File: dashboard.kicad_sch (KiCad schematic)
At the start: 38 parts, among them J2 Conn_01x02, J3 RJ45, J4 Conn_01x10, J5 776267-1, Q1 2N7002, SW1 SW_Push, SW2 SW_SPST, SW4 SW_SPST, U1 TPS542025DDC, U2 R-78C5.0-1.0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

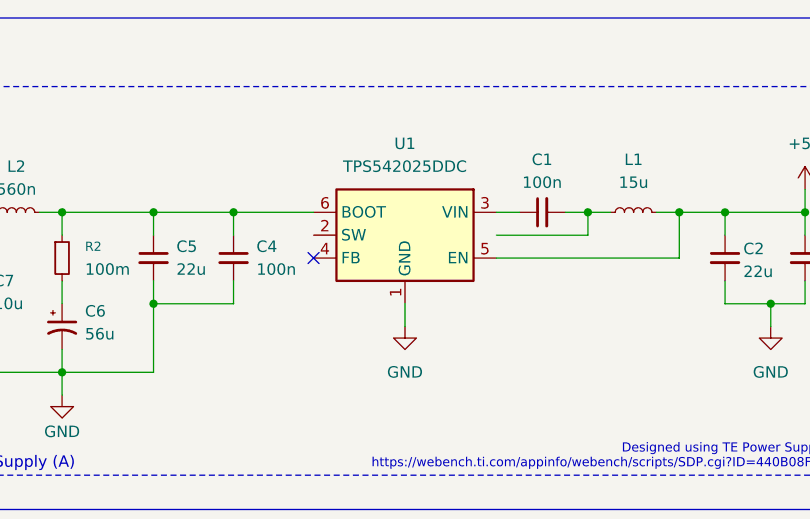
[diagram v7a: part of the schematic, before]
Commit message: Revert "added thermal vias for TPS54"
This reverts commit a34f3b064daca832ff572b55e7f0ad72ed936012.
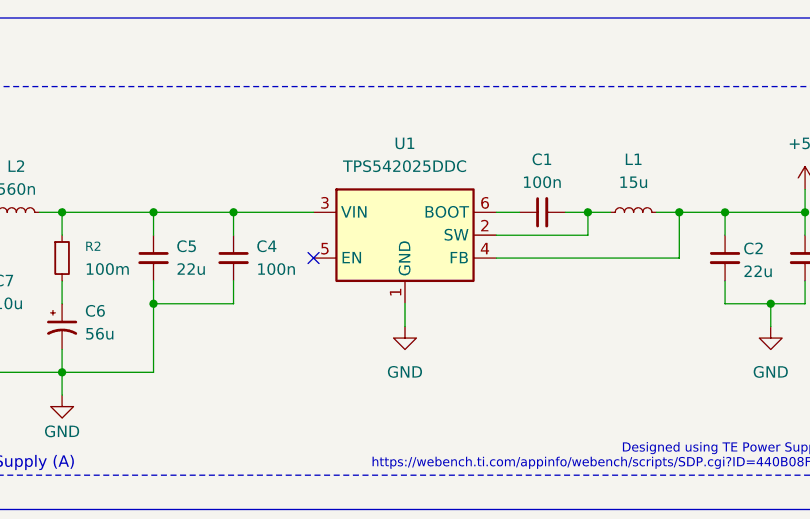
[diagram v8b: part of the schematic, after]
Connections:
- net +5V: now also U1.4 (FB); no longer U1.5 (EN)
- net at C4.1, C5.1, L2.2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: now also U1.3 (VIN); no longer U1.6 (BOOT)
- net at U1.2 (SW): now also C1.2, L1.1
- net at C1.1: now also U1.6 (BOOT); no longer U1.3 (VIN)
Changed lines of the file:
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@@
 		(lib_id "Regulator_Switching:TPS54202DDC")
 		(at 105.41 40.64 0)
-		(mirror y)
-		(unit 1)
-		(exclude_from_sim no)
-		(in_bom yes)
-		(on_board yes)
-		(dnp no)
+		(unit 1)
+		(exclude_from_sim no)
+		(in_bom yes)
+		(on_board yes)
+		(dnp no)
+		(fields_autoplaced yes)
 		(property "Reference" "U1"
 			(at 105.41 30.48 0)
@@
 		)
 		(property "Footprint" "Package_TO_SOT_SMD:SOT-23-6"
-			(at 104.14 49.53 0)
+			(at 106.68 49.53 0)
 			(effects
 				(font
@@
 		)
 		(property "Datasheet" "http://www.ti.com/lit/ds/symlink/tps54202.pdf"
-			(at 113.03 31.75 0)
+			(at 97.79 31.75 0)
 			(effects
 				(font
@@
 		)
 		(instances
-			(project "dashboard"
+			(project ""
 				(path "/e03820ab-31df-4dd3-bbbf-004e9f7c6b92"
 					(reference "#PWR024")
